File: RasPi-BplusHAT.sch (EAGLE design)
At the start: 10 parts, among them K2 RASPI_HEADER

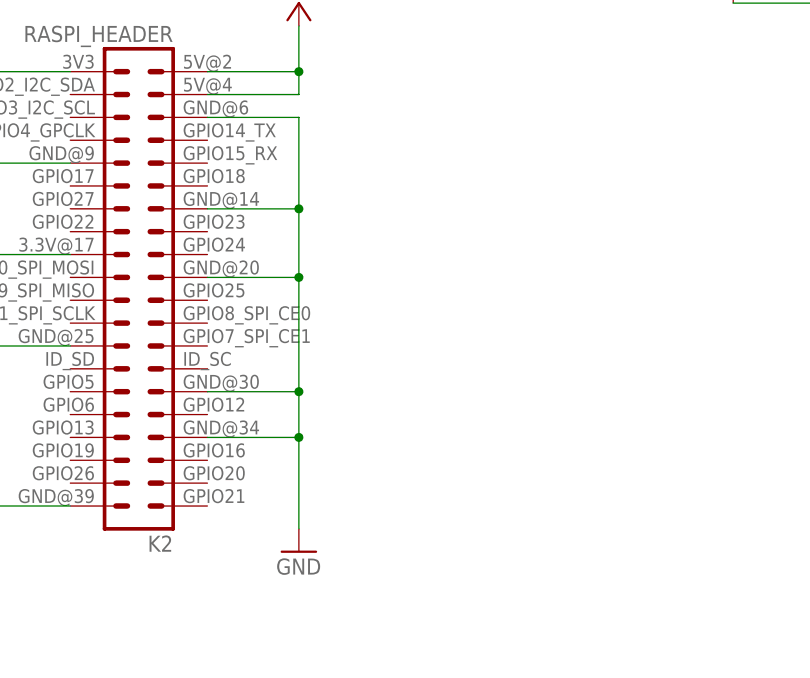
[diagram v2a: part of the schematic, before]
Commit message: hook up digo pins to gpios
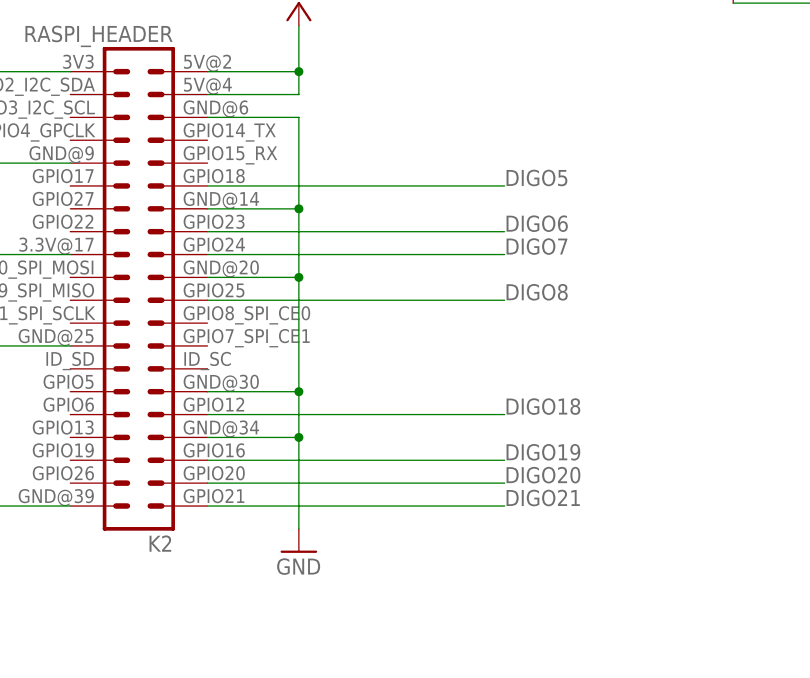
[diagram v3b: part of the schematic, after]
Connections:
- net DIGO18: now also K2.32
- net DIGO19: now also K2.36
- net DIGO20: now also K2.38
- net DIGO21: now also K2.GPIO21
- net DIGO5: now also K2.12
- net DIGO6: now also K2.16
- net DIGO7: now also K2.18
- net DIGO8: now also K2.22
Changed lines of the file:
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@@
 <wire x1="185.42" y1="190.5" x2="210.82" y2="190.5" width="0.1524" layer="91"/>
+</segment>
+<segment>
+<pinref part="K2" gate="G$1" pin="12"/>
+<wire x1="58.42" y1="162.56" x2="91.44" y2="162.56" width="0.1524" layer="91"/>
+<label x="91.44" y="162.56" size="1.778" layer="95"/>
 </segment>
 </net>
@@
 <pinref part="R2" gate="G$1" pin="1"/>
 </segment>
+<segment>
+<pinref part="K2" gate="G$1" pin="16"/>
+<wire x1="58.42" y1="157.48" x2="91.44" y2="157.48" width="0.1524" layer="91"/>
+<label x="91.44" y="157.48" size="1.778" layer="95"/>
+</segment>
 </net>
 <net name="DIGO7" class="0">
@@
 <pinref part="R3" gate="G$1" pin="1"/>
 </segment>
+<segment>
+<pinref part="K2" gate="G$1" pin="18"/>
+<wire x1="58.42" y1="154.94" x2="91.44" y2="154.94" width="0.1524" layer="91"/>
+<label x="91.44" y="154.94" size="1.778" layer="95"/>
+</segment>
 </net>
 <net name="DIGO8" class="0">
@@
 <wire x1="185.42" y1="182.88" x2="228.6" y2="182.88" width="0.1524" layer="91"/>
 <pinref part="R4" gate="G$1" pin="1"/>
+</segment>
+<segment>
+<pinref part="K2" gate="G$1" pin="22"/>
+<wire x1="58.42" y1="149.86" x2="91.44" y2="149.86" width="0.1524" layer="91"/>
+<label x="91.44" y="149.86" size="1.778" layer="95"/>
 </segment>
 </net>
@@
 <pinref part="R5" gate="G$1" pin="1"/>
 </segment>
+<segment>
+<pinref part="K2" gate="G$1" pin="32"/>
+<wire x1="58.42" y1="137.16" x2="91.44" y2="137.16" width="0.1524" layer="91"/>
+<label x="91.44" y="137.16" size="1.778" layer="95"/>
+</segment>
 </net>
 <net name="DIGO19" class="0">
@@
 <wire x1="170.18" y1="187.96" x2="132.08" y2="187.96" width="0.1524" layer="91"/>
 <pinref part="R6" gate="G$1" pin="1"/>
+</segment>
+<segment>
+<pinref part="K2" gate="G$1" pin="36"/>
+<wire x1="58.42" y1="132.08" x2="91.44" y2="132.08" width="0.1524" layer="91"/>
+<label x="91.44" y="132.08" size="1.778" layer="95"/>
 </segment>
 </net>
@@
 <pinref part="R7" gate="G$1" pin="1"/>
 </segment>
+<segment>
+<pinref part="K2" gate="G$1" pin="38"/>
+<wire x1="58.42" y1="129.54" x2="91.44" y2="129.54" width="0.1524" layer="91"/>
+<label x="91.44" y="129.54" size="1.778" layer="95"/>
+</segment>
 </net>
 <net name="DIGO21" class="0">
@@
 <pinref part="R8" gate="G$1" pin="1"/>
 </segment>
+<segment>
+<pinref part="K2" gate="G$1" pin="GPIO21"/>
+<wire x1="58.42" y1="127" x2="91.44" y2="127" width="0.1524" layer="91"/>
+<label x="91.44" y="127" size="1.778" layer="95"/>
+</segment>
 </net>

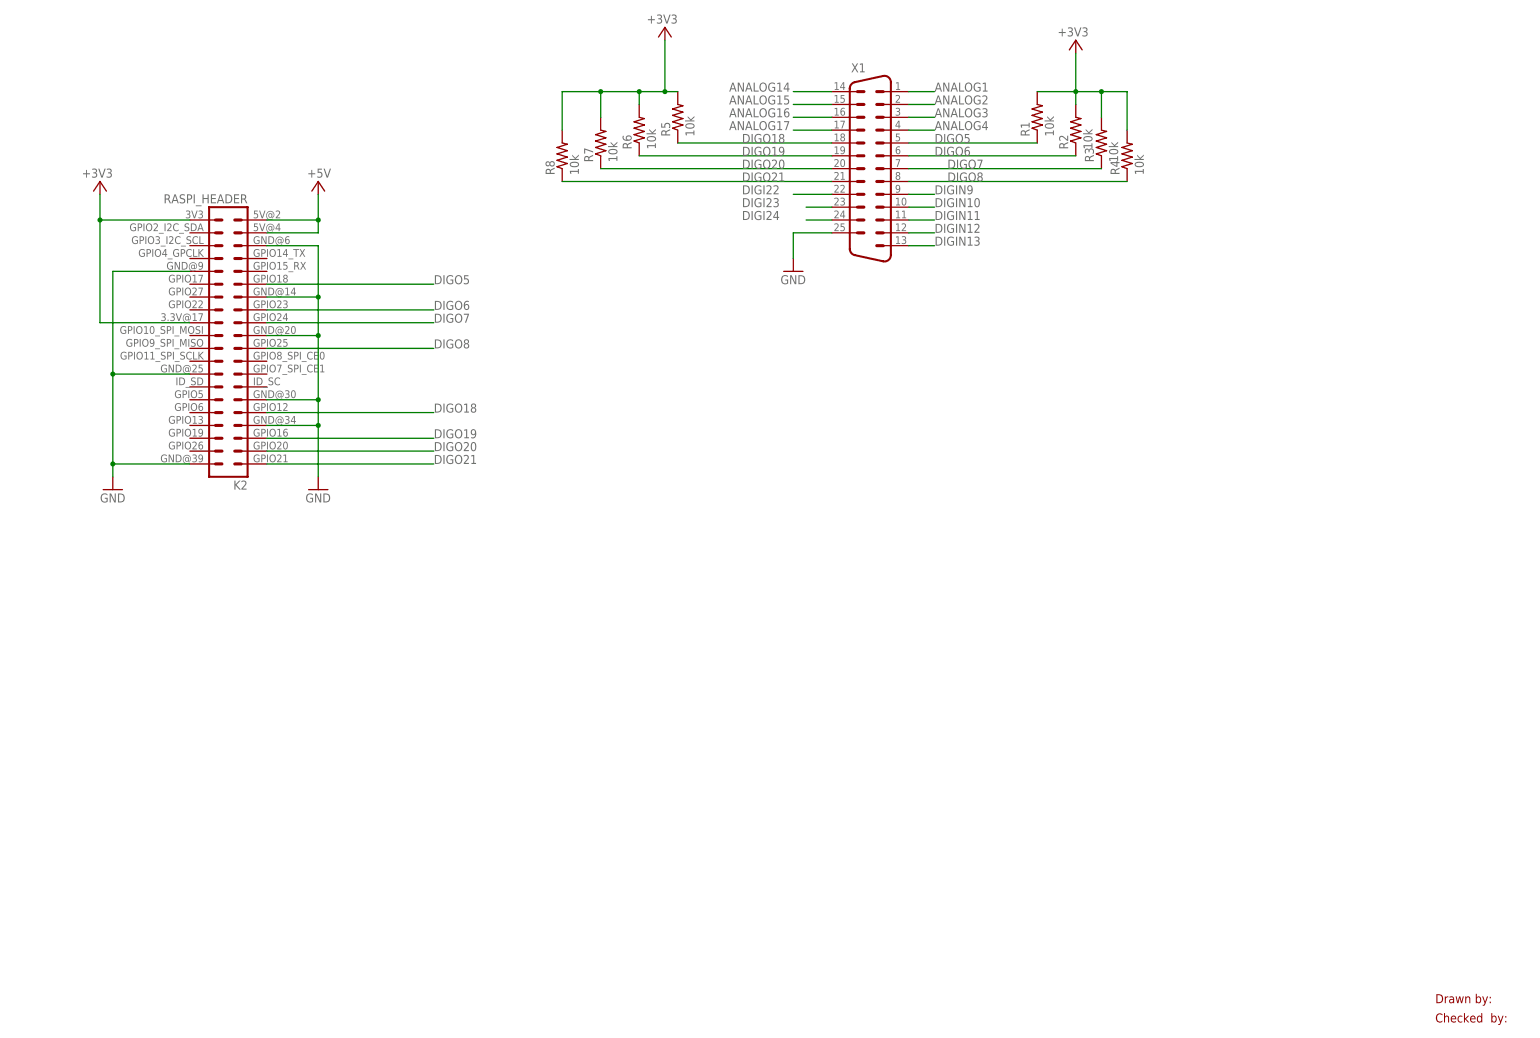
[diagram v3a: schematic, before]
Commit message: add level shifter
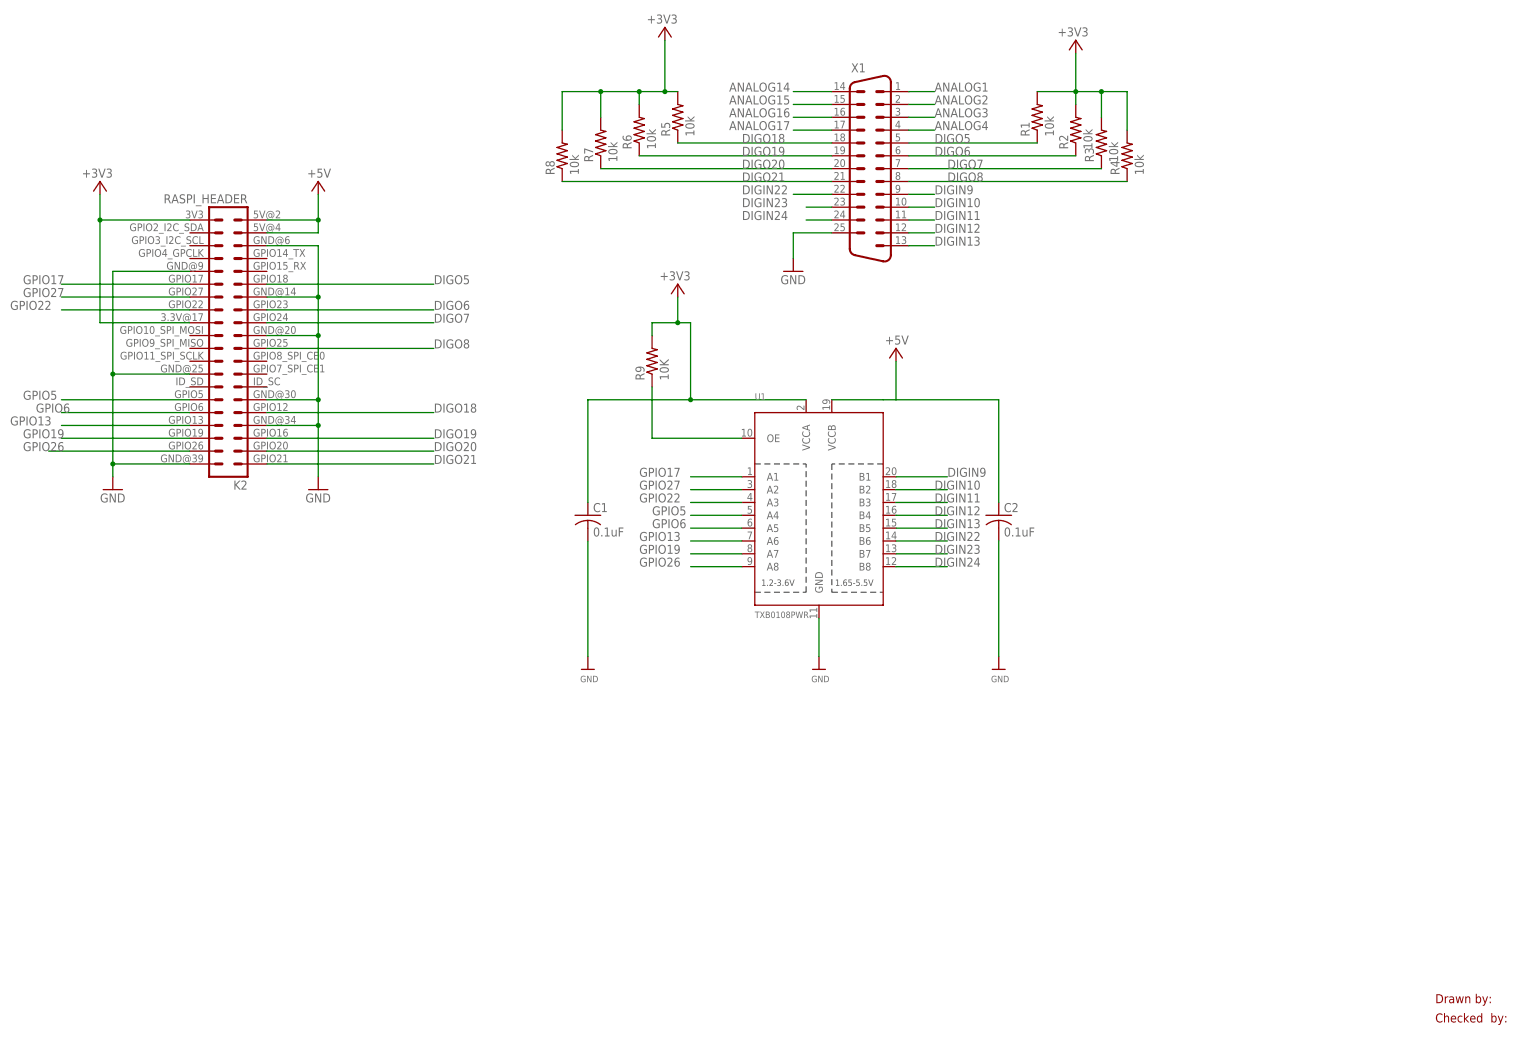
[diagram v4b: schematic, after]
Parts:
- added C1, C2: 0.1uF, adafruit:C-USC0805
- added R9: 10K, adafruit:R-US_R0805
- added U1: TXB0108PWR, microbuilder:TXB0108PWR
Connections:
- removed net DIGI22: X1G$1.22
- removed net DIGI23: X1G$1.23
- removed net DIGI24: X1G$1.24
- new net DIGIN22: U1.B6, X1G$1.22
- new net DIGIN23: U1.B7, X1G$1.23
- new net DIGIN24: U1.B8, X1G$1.24
- new net GPIO13: K2.33, U1.A6
- new net GPIO17: K2.11, U1.A1
- new net GPIO19: K2.35, U1.A7
- new net GPIO22: K2.15, U1.A3
- new net GPIO26: K2.37, U1.A8
- new net GPIO27: K2.13, U1.A2
- new net GPIO5: K2.29, U1.A4
- new net GPIO6: K2.31, U1.A5
- new net N$20: R9.1, U1.OE
- net +3V3: now also C1.1, R9.2, U1.VCCA
- net +5V: now also C2.1, U1.VCCB
- net DIGIN10: now also U1.B2
- net DIGIN11: now also U1.B3
- net DIGIN12: now also U1.B4
- net DIGIN13: now also U1.B5
- net DIGIN9: now also U1.B1
- net GND: now also C1.2, C2.2, U1.GND

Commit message: re-route
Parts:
- removed C2: 0.1uF, adafruit:C-USC0805
- added C3: .1 uF, SparkFun-Capacitors:0.1UF-50V-20%(PTH)KIT-EZ
- C1: value 0.1uF -> .1 uF; device adafruit:C-USC0805 -> SparkFun-Capacitors:0.1UF-50V-20%(PTH)KIT-EZ
- R9: value 10K -> 10k; device adafruit:R-US_R0805 -> resistor:R-US_0207/10
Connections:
- net +3V3: now also C3.1; no longer C1.1
- net +5V: now also C1.1; no longer C2.1
- net GND: now also C3.2; no longer C2.2
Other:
- moved on the sheet: C1
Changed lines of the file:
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@@
 <layer number="123" name="tTestmark" color="7" fill="1" visible="no" active="yes"/>
 <layer number="124" name="bTestmark" color="7" fill="1" visible="no" active="yes"/>
+<layer number="125" name="_tNames" color="7" fill="1" visible="no" active="yes"/>
 <layer number="131" name="tAdjust" color="7" fill="1" visible="no" active="yes"/>
 <layer number="132" name="bAdjust" color="7" fill="1" visible="no" active="yes"/>
@@
 <layer number="209" name="209bmp" color="7" fill="1" visible="no" active="yes"/>
 <layer number="210" name="210bmp" color="7" fill="1" visible="no" active="yes"/>
+<layer number="211" name="211bmp" color="7" fill="1" visible="no" active="yes"/>
+<layer number="212" name="212bmp" color="7" fill="1" visible="no" active="yes"/>
+<layer number="213" name="213bmp" color="7" fill="1" visible="no" active="yes"/>
+<layer number="214" name="214bmp" color="7" fill="1" visible="no" active="yes"/>
+<layer number="215" name="215bmp" color="7" fill="1" visible="no" active="yes"/>
+<layer number="216" name="216bmp" color="7" fill="1" visible="no" active="yes"/>
+<layer number="217" name="217bmp" color="18" fill="1" visible="no" active="no"/>
+<layer number="218" name="218bmp" color="19" fill="1" visible="no" active="no"/>
+<layer number="219" name="219bmp" color="20" fill="1" visible="no" active="no"/>
+<layer number="220" name="220bmp" color="21" fill="1" visible="no" active="no"/>
+<layer number="221" name="221bmp" color="22" fill="1" visible="no" active="no"/>
+<layer number="222" name="222bmp" color="23" fill="1" visible="no" active="no"/>
+<layer number="223" name="223bmp" color="24" fill="1" visible="no" active="no"/>
+<layer number="224" name="224bmp" color="25" fill="1" visible="no" active="no"/>
 <layer number="250" name="Descript" color="7" fill="1" visible="yes" active="yes"/>
 <layer number="251" name="SMDround" color="7" fill="1" visible="yes" active="yes"/>
@@
 <part name="U$3" library="microbuilder" deviceset="GND" device=""/>
 <part name="U1" library="microbuilder" deviceset="TXB0108PWR" device="" value="TXB0108PWR"/>
-<part name="C1" library="adafruit" deviceset="C-US" device="C0805" value="0.1uF"/>
-<part name="C2" library="adafruit" deviceset="C-US" device="C0805" value="0.1uF"/>
-<part name="R9" library="adafruit" deviceset="R-US_" device="R0805" value="10K"/>
 <part name="P+2" library="supply1" deviceset="+5V" device=""/>
 <part name="+3V4" library="supply1" deviceset="+3V3" device=""/>
+<part name="R9" library="resistor" deviceset="R-US_" device="0207/10" value="10k"/>
+<part name="C3" library="SparkFun-Capacitors" deviceset="0.1UF-50V-20%(PTH)" device="KIT-EZ" value=".1 uF"/>
+<part name="C1" library="SparkFun-Capacitors" deviceset="0.1UF-50V-20%(PTH)" device="KIT-EZ" value=".1 uF"/>
 </parts>
 <sheets>
@@
 <instance part="U$3" gate="G$1" x="203.2" y="86.36"/>
 <instance part="U1" gate="G$1" x="167.64" y="119.38"/>
-<instance part="C1" gate="G$1" x="121.92" y="116.84"/>
-<instance part="C2" gate="G$1" x="203.2" y="116.84"/>
-<instance part="R9" gate="G$1" x="134.62" y="147.32" rot="R90"/>
 <instance part="P+2" gate="1" x="182.88" y="149.86" smashed="yes">
 <attribute name="VALUE" x="185.42" y="152.4" size="1.778" layer="96" rot="R180"/>
@@
 <attribute name="VALUE" x="142.24" y="165.1" size="1.778" layer="96" rot="R180"/>
 </instance>
+<instance part="R9" gate="G$1" x="134.62" y="147.32" rot="R90"/>
+<instance part="C3" gate="G$1" x="121.92" y="114.3"/>
+<instance part="C1" gate="G$1" x="203.2" y="114.3"/>
 </instances>
 <busses>
@@
 <wire x1="121.92" y1="111.76" x2="121.92" y2="88.9" width="0.1524" layer="91"/>
 <pinref part="U$2" gate="G$1" pin="GND"/>
-<pinref part="C1" gate="G$1" pin="2"/>
+<pinref part="C3" gate="G$1" pin="2"/>
 </segment>
 <segment>
 <wire x1="203.2" y1="111.76" x2="203.2" y2="88.9" width="0.1524" layer="91"/>
 <pinref part="U$3" gate="G$1" pin="GND"/>
-<pinref part="C2" gate="G$1" pin="2"/>
+<pinref part="C1" gate="G$1" pin="2"/>
 </segment>
 <segment>
@@
 <junction x="142.24" y="139.7"/>
 <pinref part="U1" gate="G$1" pin="VCCA"/>
-<pinref part="C1" gate="G$1" pin="1"/>
-<pinref part="R9" gate="G$1" pin="2"/>
 <wire x1="139.7" y1="154.94" x2="139.7" y2="160.02" width="0.1524" layer="91"/>
 <junction x="139.7" y="154.94"/>
 <pinref part="+3V4" gate="G$1" pin="+3V3"/>
+<pinref part="R9" gate="G$1" pin="2"/>
+<pinref part="C3" gate="G$1" pin="1"/>
 </segment>
 </net>
@@
 <segment>
 <wire x1="203.2" y1="139.7" x2="203.2" y2="119.38" width="0.1524" layer="91"/>
-<wire x1="170.18" y1="139.7" x2="180.34" y2="139.7" width="0.1524" layer="91"/>
-<pinref part="C2" gate="G$1" pin="1"/>
+<wire x1="170.18" y1="139.7" x2="182.88" y2="139.7" width="0.1524" layer="91"/>
 <pinref part="U1" gate="G$1" pin="VCCB"/>
 <wire x1="182.88" y1="139.7" x2="203.2" y2="139.7" width="0.1524" layer="91"/>
-<wire x1="180.34" y1="139.7" x2="182.88" y2="139.7" width="0.1524" layer="91"/>
 <wire x1="182.88" y1="139.7" x2="182.88" y2="147.32" width="0.1524" layer="91"/>
 <pinref part="P+2" gate="1" pin="+5V"/>
+<pinref part="C1" gate="G$1" pin="1"/>
 </segment>
 </net>
